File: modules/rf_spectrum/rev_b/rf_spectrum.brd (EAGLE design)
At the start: 68.1 x 66 mm, 46 parts, among them J3 SIGNPOST_DEBUG_HEADERSMT, J4 SIGNPOST_MODULE_HEADER, J5 TC2030-JLINK-L, Q1 SI223DDS, U1 MWSUB3G, U2 SKY13317, U3 STM32L432KC, U4 TLV62130, X1 ABS05-32.768KHZ-T

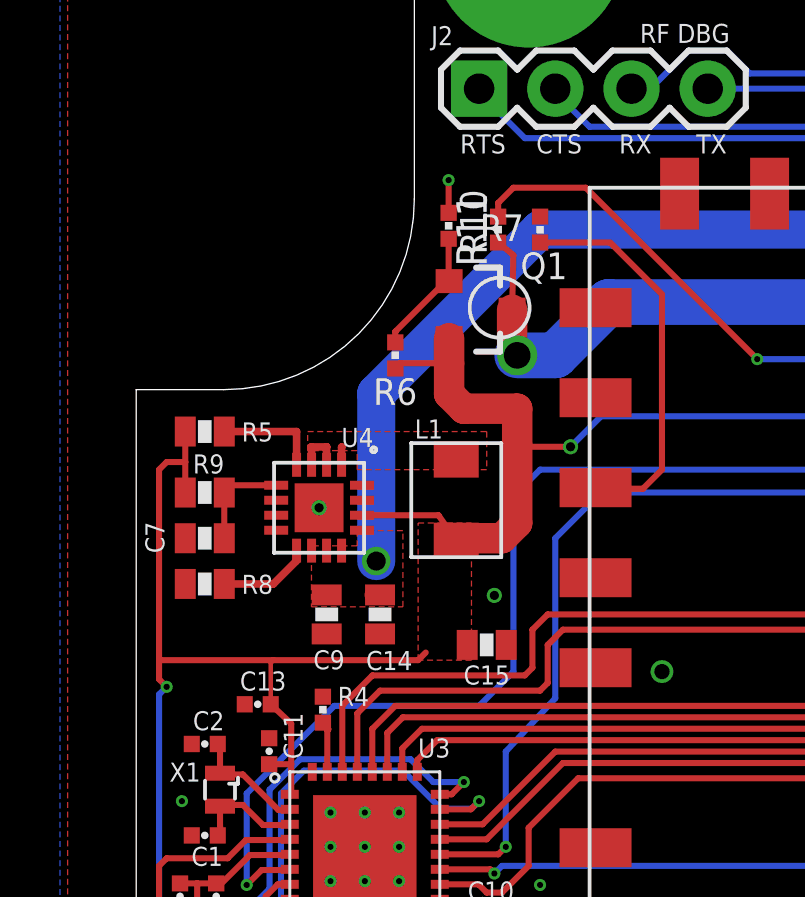
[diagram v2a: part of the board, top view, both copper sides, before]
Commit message: renumbered componenets, added BOM
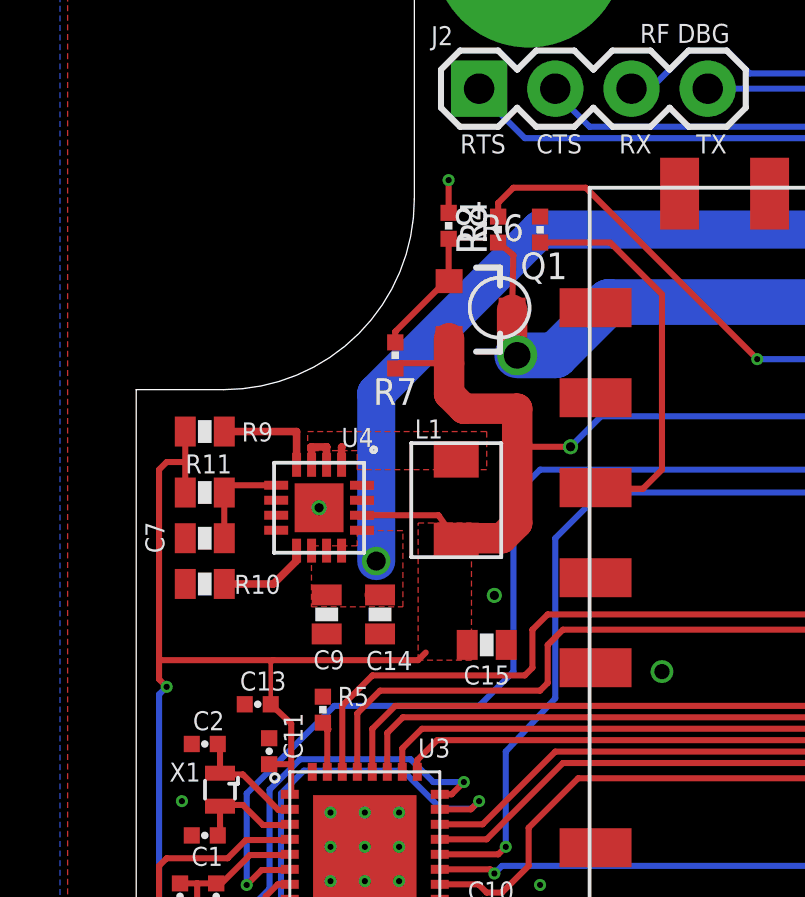
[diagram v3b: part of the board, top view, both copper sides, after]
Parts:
- R10: value 1k -> 240k; device passives:0402_RES -> passives:0603-RES
- R11: value 100k -> 750k; device passives:0402_RES -> passives:0603-RES
- R4: value 10k -> 1k
- R5: value 100k -> 10k; device passives:0603-RES -> passives:0402_RES
- R8: value 240k -> 100k; device passives:0603-RES -> passives:0402_RES
- R9: value 750k -> 100k
- moved R4 16.7 mm to (13.0, 55.6), turned to 90 degrees
- moved R8 14.2 mm to (14.6, 55.5), turned to 90 degrees
- moved R10 13.2 mm to (4.83, 45.2), turned to 0 degrees
- moved R11 13.1 mm to (4.83, 46.7), turned to 180 degrees
- moved R5 10.1 mm to (8.76, 39.5), turned to 270 degrees
- moved R6 6.39 mm to (16.0, 55.5), turned to 90 degrees
- moved R7 6.39 mm to (11.2, 51.3), turned to 270 degrees
- moved R9 2.03 mm to (4.83, 48.8)
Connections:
- net 3V3: now also R11.2, R7.2; no longer R5.2, R6.2
- net GATED: now also R8.1; no longer R11.1
- net GND: now also R10.1, R5.1, R6.2; no longer R4.1, R7.2, R8.1
- net N$11: now also R5.2; no longer R4.2
- net N$13: now also R4.1, R7.1; no longer R10.1, R6.1
- net N$36: now also R9.1; no longer R5.1
- net N$37: now also R10.2, R11.1; no longer R8.2, R9.1
- net POWER_GATE: now also R4.2; no longer R10.2
- net RF_GPIO2: now also R6.1; no longer R7.1
- net RF_GPIO3: now also R8.2; no longer R11.2
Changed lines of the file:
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@@
 <setting verticaltext="up"/>
 </settings>
-<grid distance="5" unitdist="mil" unit="mil" style="lines" multiple="1" display="yes" altdistance="10" altunitdist="mil" altunit="mil"/>
+<grid distance="100" unitdist="mil" unit="mil" style="lines" multiple="1" display="yes" altdistance="10" altunitdist="mil" altunit="mil"/>
 <layers>
 <layer number="1" name="Top" color="4" fill="1" visible="yes" active="yes"/>
@@
 <attribute name="NAME" x="14.224" y="40.3352" size="0.635" layer="25" font="vector" ratio="12" align="bottom-center"/>
 </element>
-<element name="R9" library="passives" package="0603-RES" value="750k" x="4.826" y="46.736" smashed="yes" rot="R180">
+<element name="R11" library="passives" package="0603-RES" value="750k" x="4.826" y="46.736" smashed="yes" rot="R180">
 <attribute name="DIGIKEY" value="311-750KGRCT-ND" x="4.826" y="46.736" size="1.778" layer="27" rot="R180" display="off"/>
 <attribute name="MANUFACTURER" value="Yageo" x="4.826" y="46.736" size="1.778" layer="27" rot="R180" display="off"/>
@@
 <attribute name="NAME" x="4.953" y="48.006" size="0.635" layer="25" font="vector" ratio="12" rot="R180" align="bottom-center"/>
 </element>
-<element name="R8" library="passives" package="0603-RES" value="240k" x="4.826" y="45.212" smashed="yes">
+<element name="R10" library="passives" package="0603-RES" value="240k" x="4.826" y="45.212" smashed="yes">
 <attribute name="DIGIKEY" value="311-240KGRCT-ND" x="4.826" y="45.212" size="1.778" layer="27" display="off"/>
 <attribute name="MANUFACTURER" value="Yageo" x="4.826" y="45.212" size="1.778" layer="27" display="off"/>
@@
 <attribute name="NAME" x="6.5786" y="43.3578" size="0.635" layer="25" font="vector" ratio="12" align="bottom-center"/>
 </element>
-<element name="R5" library="passives" package="0603-RES" value="100k" x="4.826" y="48.768" smashed="yes" rot="R180">
+<element name="R9" library="passives" package="0603-RES" value="100k" x="4.826" y="48.768" smashed="yes" rot="R180">
 <attribute name="DIGIKEY" value="311-100KGRCT-ND" x="4.826" y="48.768" size="1.778" layer="27" rot="R180" display="off"/>
 <attribute name="MANUFACTURER" value="Yageo" x="4.826" y="48.768" size="1.778" layer="27" rot="R180" display="off"/>
@@
 <attribute name="VALUE" x="50.2412" y="56.9722" size="1.27" layer="27"/>
 </element>
-<element name="R7" library="passives" package="0402_RES" value="100k" x="16.002" y="55.499" smashed="yes" rot="R90">
+<element name="R6" library="passives" package="0402_RES" value="100k" x="16.002" y="55.499" smashed="yes" rot="R90">
 <attribute name="DIGIKEY" value="311-100KLRCT-ND" x="16.002" y="55.499" size="1.778" layer="27" font="vector" ratio="12" rot="R90" display="off"/>
 <attribute name="MANUFACTURER" value="Yageo" x="16.002" y="55.499" size="1.778" layer="27" font="vector" ratio="12" rot="R90" display="off"/>
@@
 <attribute name="VALUE" x="17.399" y="55.499" size="1.016" layer="27" font="vector" ratio="12" rot="R90" align="bottom-center"/>
 </element>
-<element name="R4" library="passives" package="0402_RES" value="10k" x="8.763" y="39.497" smashed="yes" rot="R270">
+<element name="R5" library="passives" package="0402_RES" value="10k" x="8.763" y="39.497" smashed="yes" rot="R270">
 <attribute name="DIGIKEY" value="311-1.0KJRCT-ND" x="8.763" y="39.497" size="1.778" layer="27" font="vector" ratio="12" rot="R270" display="off"/>
 <attribute name="MANUFACTURER" value="Yageo" x="8.763" y="39.497" size="1.778" layer="27" font="vector" ratio="12" rot="R270" display="off"/>
@@
 <attribute name="NAME" x="16.129" y="53.848" size="0.889" layer="25" font="vector" ratio="12" align="bottom-center"/>
 </element>
-<element name="R6" library="passives" package="0402_RES" value="100k" x="11.176" y="51.308" smashed="yes" rot="R270">
+<element name="R7" library="passives" package="0402_RES" value="100k" x="11.176" y="51.308" smashed="yes" rot="R270">
 <attribute name="DIGIKEY" value="311-100KLRCT-ND" x="11.176" y="51.308" size="1.778" layer="27" font="vector" ratio="12" rot="R270" display="off"/>
 <attribute name="MANUFACTURER" value="Yageo" x="11.176" y="51.308" size="1.778" layer="27" font="vector" ratio="12" rot="R270" display="off"/>
@@
 <attribute name="VALUE" x="9.779" y="51.308" size="1.016" layer="27" font="vector" ratio="12" rot="R270" align="bottom-center"/>
 </element>
-<element name="R10" library="passives" package="0402_RES" value="1k" x="12.954" y="55.626" smashed="yes" rot="R90">
+<element name="R4" library="passives" package="0402_RES" value="1k" x="12.954" y="55.626" smashed="yes" rot="R90">
 <attribute name="DIGIKEY" value="311-100KLRCT-ND" x="12.954" y="55.626" size="1.778" layer="27" font="vector" ratio="12" rot="R90" display="off"/>
 <attribute name="MANUFACTURER" value="Yageo" x="12.954" y="55.626" size="1.778" layer="27" font="vector" ratio="12" rot="R90" display="off"/>
@@
 <attribute name="MPN" value="0015912080" x="36.6014" y="7.6454" size="1.778" layer="27" font="vector" ratio="12" display="off"/>
 </element>
-<element name="R11" library="passives" package="0402_RES" value="100k" x="14.605" y="55.499" rot="R90">
+<element name="R8" library="passives" package="0402_RES" value="100k" x="14.605" y="55.499" rot="R90">
 <attribute name="DIGIKEY" value="311-100KLRCT-ND" x="14.605" y="55.499" size="1.778" layer="27" font="vector" ratio="12" rot="R90" display="off"/>
 <attribute name="MANUFACTURER" value="Yageo" x="14.605" y="55.499" size="1.778" layer="27" font="vector" ratio="12" rot="R90" display="off"/>
@@
 <contactref element="U4" pad="GND"/>
 <contactref element="U4" pad="16"/>
-<contactref element="R8" pad="1"/>
+<contactref element="R10" pad="1"/>
 <contactref element="C15" pad="1"/>
 <polygon width="0.1524" layer="1" isolate="0.1524" thermals="no" rank="2">
@@
 <vertex x="-0.254" y="-9.906"/>
 </polygon>
-<contactref element="R4" pad="1"/>
+<contactref element="R5" pad="1"/>
 <via x="20.066" y="40.767" extent="1-16" drill="0.508"/>
 <via x="14.478" y="43.307" extent="1-16" drill="0.3048"/>
@@
 <contactref element="J4" pad="14"/>
 <contactref element="J4" pad="1"/>
-<contactref element="R7" pad="2"/>
+<contactref element="R6" pad="2"/>
 </signal>
 <signal name="3V3">
@@
 <contactref element="U4" pad="14"/>
 <contactref element="L1" pad="P$2"/>
-<contactref element="R5" pad="2"/>
 <contactref element="R9" pad="2"/>
+<contactref element="R11" pad="2"/>
 <contactref element="C15" pad="2"/>
 <wire x1="10.066" y1="45.974" x2="10.066" y2="45.978" width="0.254" layer="1"/>
@@
 <wire x1="17.018" y1="48.26" x2="15.285403125" y2="48.26" width="0.2032" layer="1"/>
 <wire x1="15.285403125" y1="48.26" x2="15.24" y2="48.305403125" width="0.2032" layer="1"/>
-<contactref element="R6" pad="2"/>
+<contactref element="R7" pad="2"/>
 <wire x1="13.462" y1="49.53" x2="12.97" y2="50.022" width="1.016" layer="1"/>
 <wire x1="12.97" y1="51.0441" x2="12.97" y2="50.022" width="1.016" layer="1"/>
@@
 </signal>
 <signal name="N$36">
-<contactref element="R5" pad="1"/>
+<contactref element="R9" pad="1"/>
 <contactref element="U4" pad="4"/>
 <wire x1="5.476" y1="48.768" x2="7.886" y2="48.768" width="0.254" layer="1"/>
@@
 </signal>
 <signal name="N$37">
-<contactref element="R8" pad="2"/>
-<contactref element="R9" pad="1"/>
+<contactref element="R10" pad="2"/>
+<contactref element="R11" pad="1"/>
 <contactref element="U4" pad="5"/>
 <wire x1="7.206" y1="46.978" x2="5.234" y2="46.978" width="0.2032" layer="1"/>
@@
 <signal name="RF_GPIO2">
 <contactref element="U1" pad="3"/>
-<contactref element="R7" pad="1"/>
+<contactref element="R6" pad="1"/>
 <wire x1="17.920653125" y1="46.963653125" x2="17.947" y2="46.99" width="0.2032" layer="1"/>
 <wire x1="17.920653125" y1="46.963653125" x2="17.853" y2="46.896" width="0.2032" layer="1"/>
@@
 <contactref element="U3" pad="25"/>
 <contactref element="U1" pad="37"/>
-<contactref element="R11" pad="2"/>
+<contactref element="R8" pad="2"/>
 <wire x1="11.91" y1="37.425" x2="11.91" y2="37.818" width="0.2032" layer="1"/>
 <wire x1="12.573" y1="38.481" x2="29.591" y2="38.481" width="0.2032" layer="1"/>
@@
 <wire x1="8.91" y1="37.425" x2="8.91" y2="38.810253125" width="0.2032" layer="1"/>
 <wire x1="8.945559375" y1="38.8458125" x2="8.91" y2="38.810253125" width="0.2032" layer="1"/>
-<contactref element="R4" pad="2"/>
+<contactref element="R5" pad="2"/>
 <wire x1="8.763" y1="39.06393125" x2="8.763" y2="39.028371875" width="0.2032" layer="1"/>
 <wire x1="8.763" y1="39.028371875" x2="8.945559375" y2="38.8458125" width="0.2032" layer="1"/>
@@
 <wire x1="56.388" y1="50.038" x2="59.311" y2="50.038" width="1.524" layer="1"/>
 <wire x1="59.311" y1="50.038" x2="59.453" y2="49.896" width="1.524" layer="1"/>
-<contactref element="R11" pad="1"/>
+<contactref element="R8" pad="1"/>
 <wire x1="14.605" y1="55.06593125" x2="15.113" y2="54.653" width="0.2032" layer="1"/>
 <wire x1="15.113" y1="54.653" x2="15.07" y2="52.832" width="0.2032" layer="1"/>
@@
 <via x="12.954" y="57.15" extent="1-16" drill="0.2032"/>
 <wire x1="6.858" y1="33.274" x2="6.858" y2="30.48" width="0.2032" layer="1"/>
-<contactref element="R10" pad="2"/>
+<contactref element="R4" pad="2"/>
 <wire x1="12.954" y1="57.15" x2="12.954" y2="56.05906875" width="0.2032" layer="1"/>
 </signal>
 <signal name="N$13">
 <contactref element="Q1" pad="1"/>
-<contactref element="R10" pad="1"/>
-<contactref element="R6" pad="1"/>
+<contactref element="R4" pad="1"/>
+<contactref element="R7" pad="1"/>
 <wire x1="12.954" y1="53.877196875" x2="12.954" y2="55.19293125" width="0.2032" layer="1"/>
 <wire x1="12.954" y1="53.877196875" x2="12.954" y2="53.798" width="0.2032" layer="1"/>
